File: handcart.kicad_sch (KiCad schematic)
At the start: 51 parts, among them J1 ROTARY ENCODER, J10 SPARE_SUPPLY, J12 SPARE_CHARGER, J13 SPARE_BMS, J14 ADD_FAN, J15 EXT_SCREEN, J16 CHARGER, J17 BMS, J2 ARROW_KEYS_1, J3 ARROW_KEYS_2, J4 ARROW_KEYS_3, J5 ARROW_KEYS_4, J6 RESET_BUTTON, J7 TSMS, J8 MUSHROOM, J9 POWER_IN, Q1 SSM3K361TU,LF, Q17 FQP17P06, U1 Tex_DCDC_v2, U2 DCDC2510

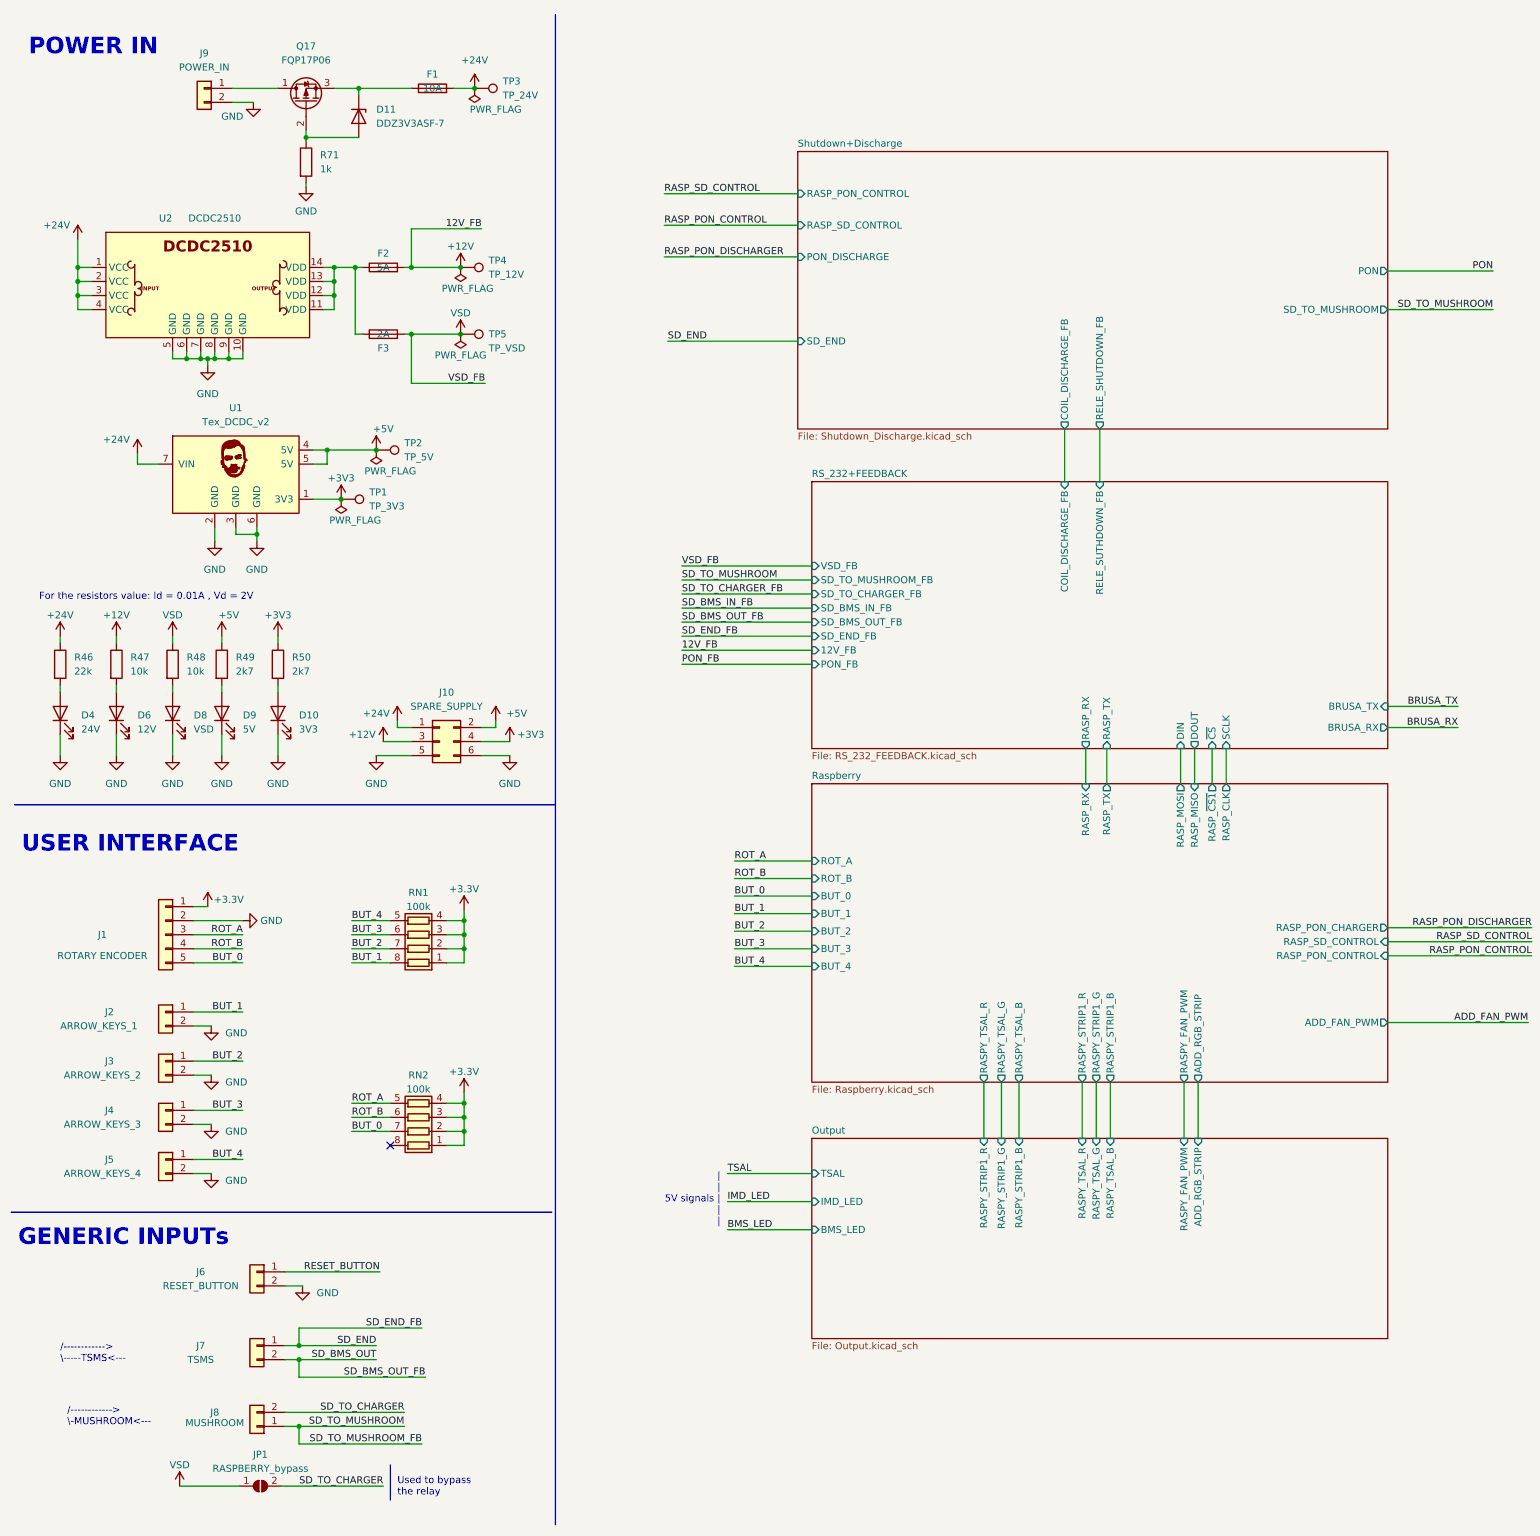
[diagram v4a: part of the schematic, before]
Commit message: Second iteration of the board layout. Need to fix some traces
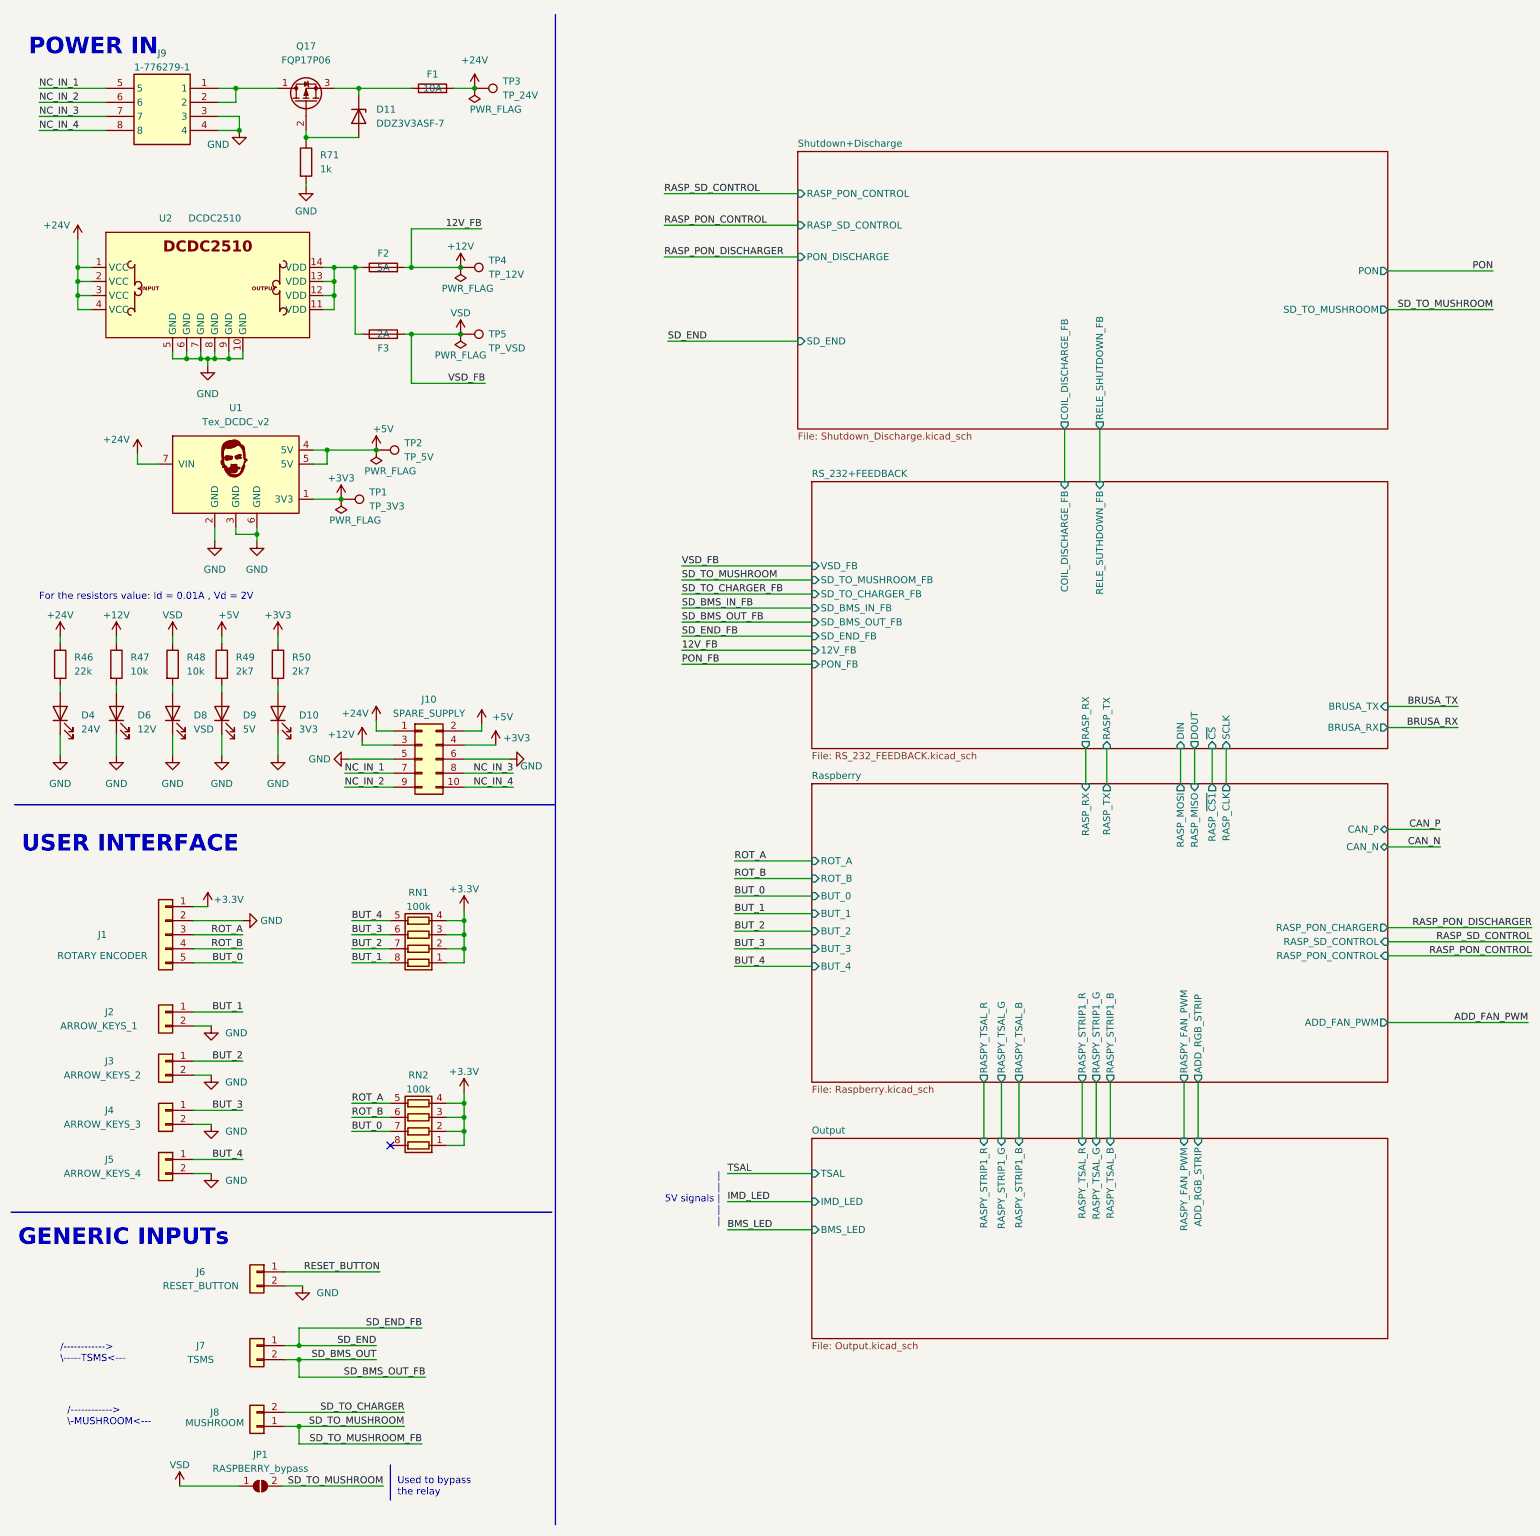
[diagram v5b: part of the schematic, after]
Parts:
- removed J9: POWER_IN, Connector_Molex:Molex_Micro-Fit_3.0_43650-0200_1x02_P3.00mm_Horizontal, symbol Connector_Generic:Conn_01x02
- added J9: 1-776279-1, Eagle_Connectors:17762791, symbol 00_proj-lib:1-776279-1
- J10: footprint Connector_Molex:Molex_Micro-Fit_3.0_43045-0612_2x03_P3.00mm_Vertical -> Connector_Molex:Molex_Micro-Fit_3.0_43045-1012_2x05_P3.00mm_Vertical; symbol Connector_Generic:Conn_02x03_Odd_Even -> Connector_Generic:Conn_02x05_Odd_Even
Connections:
- net GND: now also J9.3, J9.4
- net SD_TO_CHARGER: no longer JP1.2 (B)
- net SD_TO_MUSHROOM: now also JP1.2 (B)
- net at Q17.1 (D): now also J9.1, J9.2
- new net NC_IN_1: J10.7 (Pin_7), J9.5
- new net NC_IN_2: J10.9 (Pin_9), J9.6
- new net NC_IN_3: J10.8 (Pin_8), J9.7
- new net NC_IN_4: J10.10 (Pin_10), J9.8
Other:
- sheet Raspberry ports: added CAN_N, CAN_P; removed none

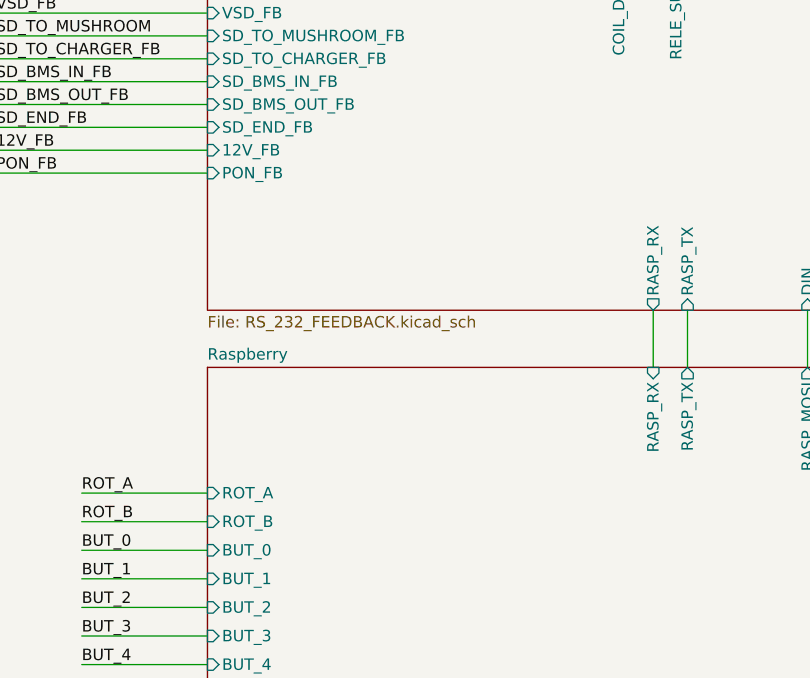
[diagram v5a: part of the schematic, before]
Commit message: Added connector, fixed traces, first version of silkscreen
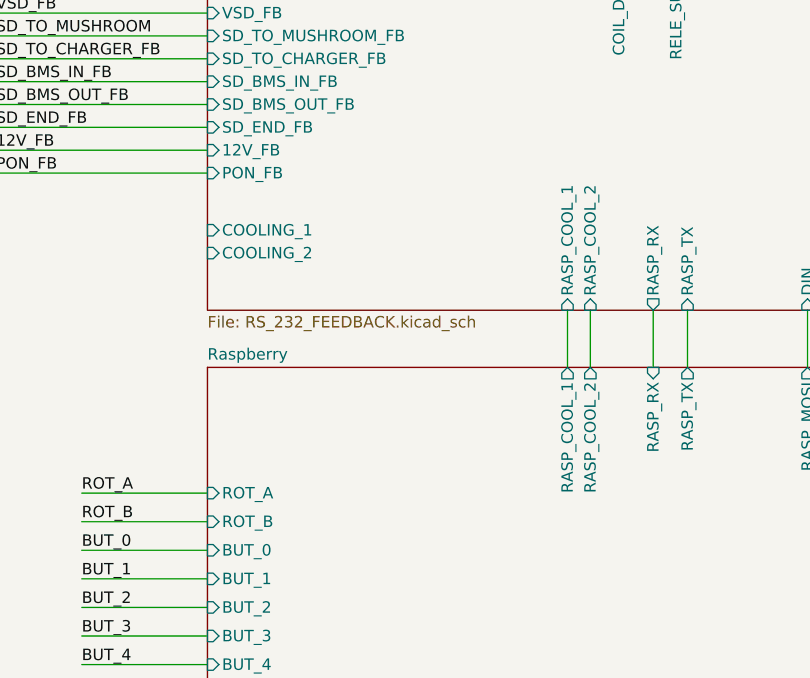
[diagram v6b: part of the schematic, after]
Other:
- sheet RS_232+FEEDBACK ports: added COOLING_1, COOLING_2, RASP_COOL_1, RASP_COOL_2; removed none
- sheet Raspberry ports: added RASP_COOL_1, RASP_COOL_2; removed none
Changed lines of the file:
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@@
     (stroke (width 0) (type default) (color 0 0 0 0))
   )
+  (wire (pts (xy 198.755 144.78) (xy 198.755 151.13))
+    (stroke (width 0) (type default) (color 0 0 0 0))
+  )
   (wire (pts (xy 73.66 57.785) (xy 73.66 69.85))
     (stroke (width 0) (type default) (color 0 0 0 0))
@@
     (stroke (width 0) (type default) (color 0 0 0 0))
   )
+  (wire (pts (xy 196.215 144.78) (xy 196.215 151.13))
+    (stroke (width 0) (type default) (color 0 0 0 0))
+  )
   (wire (pts (xy 346.075 114.3) (xy 368.3 114.3))
     (stroke (width 0) (type default) (color 0 0 0 0))
@@
       (effects (font (size 1.27 1.27)) (justify right))
     )
+    (pin "RASP_COOL_2" output (at 198.755 151.13 90)
+      (effects (font (size 1.27 1.27)) (justify right))
+    )
+    (pin "RASP_COOL_1" output (at 196.215 151.13 90)
+      (effects (font (size 1.27 1.27)) (justify right))
+    )
   )
   (sheet (at 156.21 215.265) (size 104.14 36.195) (fields_autoplaced)
@@
       (effects (font (size 1.27 1.27)) (justify left))
     )
+    (pin "RASP_COOL_1" input (at 196.215 144.78 270)
+      (effects (font (size 1.27 1.27)) (justify left))
+    )
+    (pin "RASP_COOL_2" input (at 198.755 144.78 270)
+      (effects (font (size 1.27 1.27)) (justify left))
+    )
+    (pin "COOLING_1" input (at 156.21 135.89 180)
+      (effects (font (size 1.27 1.27)) (justify left))
+    )
+    (pin "COOLING_2" input (at 156.21 138.43 180)
+      (effects (font (size 1.27 1.27)) (justify left))
+    )
   )
   (sheet_instances
@@
       (reference "#PWR0150") (unit 1) (value "+3V3") (footprint "")
     )
+    (path "/c555cf80-c75c-40ac-8827-8af7ca4e4d20/bff6f55e-c468-4944-ad45-9605d5ab942e"
+      (reference "#PWR0151") (unit 1) (value "+24V") (footprint "")
+    )
+    (path "/c555cf80-c75c-40ac-8827-8af7ca4e4d20/c91c703d-cab3-4c0a-bb1a-27456bd4cbf7"
+      (reference "#PWR0152") (unit 1) (value "+24V") (footprint "")
+    )
     (path "/c555cf80-c75c-40ac-8827-8af7ca4e4d20/35ba7db2-17e9-4d72-a7c3-85ba45c0d11a"
       (reference "#PWR0153") (unit 1) (value "GND") (footprint "")
@@
       (reference "#PWR0169") (unit 1) (value "GND") (footprint "")
     )
+    (path "/c555cf80-c75c-40ac-8827-8af7ca4e4d20/57fe55a1-a4bf-4859-842a-cf8233bf68fb"
+      (reference "#PWR0170") (unit 1) (value "GND") (footprint "")
+    )
+    (path "/c555cf80-c75c-40ac-8827-8af7ca4e4d20/fdabcfa2-618c-493e-8207-378afac55c03"
+      (reference "#PWR0171") (unit 1) (value "GND") (footprint "")
+    )
     (path "/5423ac07-d0aa-443c-8aa6-dc2e9e5796c3/20a21468-72b8-4aa3-af31-6cfbf5c1d3f5"
       (reference "BZ1") (unit 1) (value "Buzzer") (footprint "Buzzer_Beeper:Buzzer_TDK_PS1240P02BT_D12.2mm_H6.5mm")
@@
     )
     (path "/5423ac07-d0aa-443c-8aa6-dc2e9e5796c3/84716d3a-19fb-4972-aac1-e3d892a72281"
-      (reference "J18") (unit 1) (value "SPARE_RASPI") (footprint "Connector_Molex:Molex_Micro-Fit_3.0_43045-0612_2x03_P3.00mm_Vertical")
+      (reference "J18") (unit 1) (value "SPARE_RASPI") (footprint "Connector_Molex:Molex_Micro-Fit_3.0_43045-0412_2x02_P3.00mm_Vertical")
     )
     (path "/5423ac07-d0aa-443c-8aa6-dc2e9e5796c3/8302046f-ec55-441d-bcd7-40f2d89ea800"
@@
       (reference "J27") (unit 1) (value "DISCHARGE_RELAY") (footprint "Connector_Molex:Molex_Micro-Fit_3.0_43650-0215_1x02_P3.00mm_Vertical")
     )
+    (path "/c555cf80-c75c-40ac-8827-8af7ca4e4d20/a6bd9b75-0937-4f4f-bf35-f064c530f633"
+      (reference "J28") (unit 1) (value "COOLING") (footprint "Eagle_Connectors:17762791")
+    )
     (path "/c555cf80-c75c-40ac-8827-8af7ca4e4d20/21573d0d-1701-4875-9d53-7ad8682cbc7b"
       (reference "J29") (unit 1) (value "SPARE_ADC") (footprint "Connector_Molex:Molex_Micro-Fit_3.0_43045-0612_2x03_P3.00mm_Vertical")
@@
       (reference "J30") (unit 1) (value "SD_END_TEST_POINT") (footprint "Connector_Molex:Molex_Micro-Fit_3.0_43650-0215_1x02_P3.00mm_Vertical")
     )
+    (path "/c555cf80-c75c-40ac-8827-8af7ca4e4d20/e43291a8-4903-4a90-9b82-1664979f32ff"
+      (reference "J31") (unit 1) (value "SPARE_GEN") (footprint "Connector_Molex:Molex_Micro-Fit_3.0_43045-0412_2x02_P3.00mm_Vertical")
+    )
     (path "/99247b88-4b04-4caf-b551-2a591db4df70"
       (reference "JP1") (unit 1) (value "RASPBERRY_bypass") (footprint "Jumper:SolderJumper-2_P1.3mm_Open_Pad1.0x1.5mm")
@@
       (reference "Q17") (unit 1) (value "FQP17P06") (footprint "Package_TO_SOT_THT:TO-220-3_Vertical")
     )
+    (path "/c555cf80-c75c-40ac-8827-8af7ca4e4d20/583bc44e-dd52-4971-b99d-ade4033efeda"
+      (reference "Q18") (unit 1) (value "SSM3K361TU,LF") (footprint "00_proj-lib:SOTFL65P210X75-3N")
+    )
+    (path "/c555cf80-c75c-40ac-8827-8af7ca4e4d20/80bd90b3-3d24-4b5a-8d17-5ee1b365e4f8"
+      (reference "Q19") (unit 1) (value "SSM3K361TU,LF") (footprint "00_proj-lib:SOTFL65P210X75-3N")
+    )
     (path "/6fea3035-a1d5-409d-bb0f-1261e231fe16"
       (reference "R1") (unit 1) (value "22R") (footprint "Resistor_SMD:R_0603_1608Metric")
@@
       (reference "R71") (unit 1) (value "1k") (footprint "Resistor_SMD:R_0603_1608Metric")
     )
+    (path "/c555cf80-c75c-40ac-8827-8af7ca4e4d20/6cd6235f-27e1-4d6c-b221-ff3dca989be3"
+      (reference "R72") (unit 1) (value "22R") (footprint "Resistor_SMD:R_0603_1608Metric")
+    )
+    (path "/c555cf80-c75c-40ac-8827-8af7ca4e4d20/c7c6bd3d-c0dc-4842-8211-cb7be9837f84"
+      (reference "R73") (unit 1) (value "22R") (footprint "Resistor_SMD:R_0603_1608Metric")
+    )
+    (path "/c555cf80-c75c-40ac-8827-8af7ca4e4d20/82047049-7645-4a9d-8473-1ae2e21502bb"
+      (reference "R74") (unit 1) (value "330k") (footprint "Resistor_SMD:R_0603_1608Metric")
+    )
+    (path "/c555cf80-c75c-40ac-8827-8af7ca4e4d20/665d30cb-85d5-4454-8e12-ce8de0604aea"
+      (reference "R75") (unit 1) (value "330k") (footprint "Resistor_SMD:R_0603_1608Metric")
+    )
+    (path "/c555cf80-c75c-40ac-8827-8af7ca4e4d20/d62d936f-8bad-447c-a212-a581e2d1b3c3"
+      (reference "R76") (unit 1) (value "R") (footprint "Resistor_SMD:R_0805_2012Metric")
+    )
+    (path "/c555cf80-c75c-40ac-8827-8af7ca4e4d20/2948f888-818a-4224-be88-83862a0f7ee5"
+      (reference "R77") (unit 1) (value "R") (footprint "Resistor_SMD:R_0805_2012Metric")
+    )
     (path "/94f0a6aa-6489-4340-8fae-f0a4bb7d6bec"
